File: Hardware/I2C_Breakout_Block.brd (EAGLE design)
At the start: 30.5 x 44.5 mm, 23 parts, among them U2 PCA9306

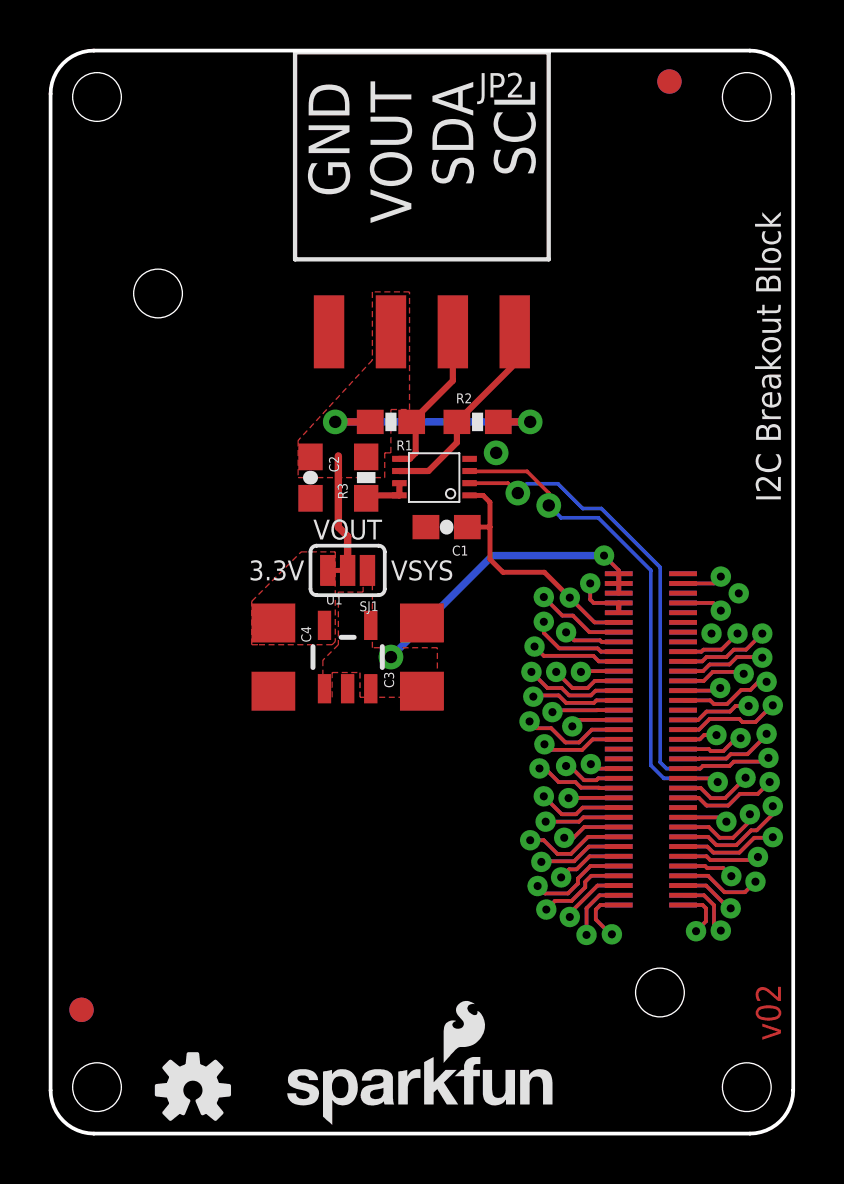
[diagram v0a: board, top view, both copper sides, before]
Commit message: repalced I2C resistors
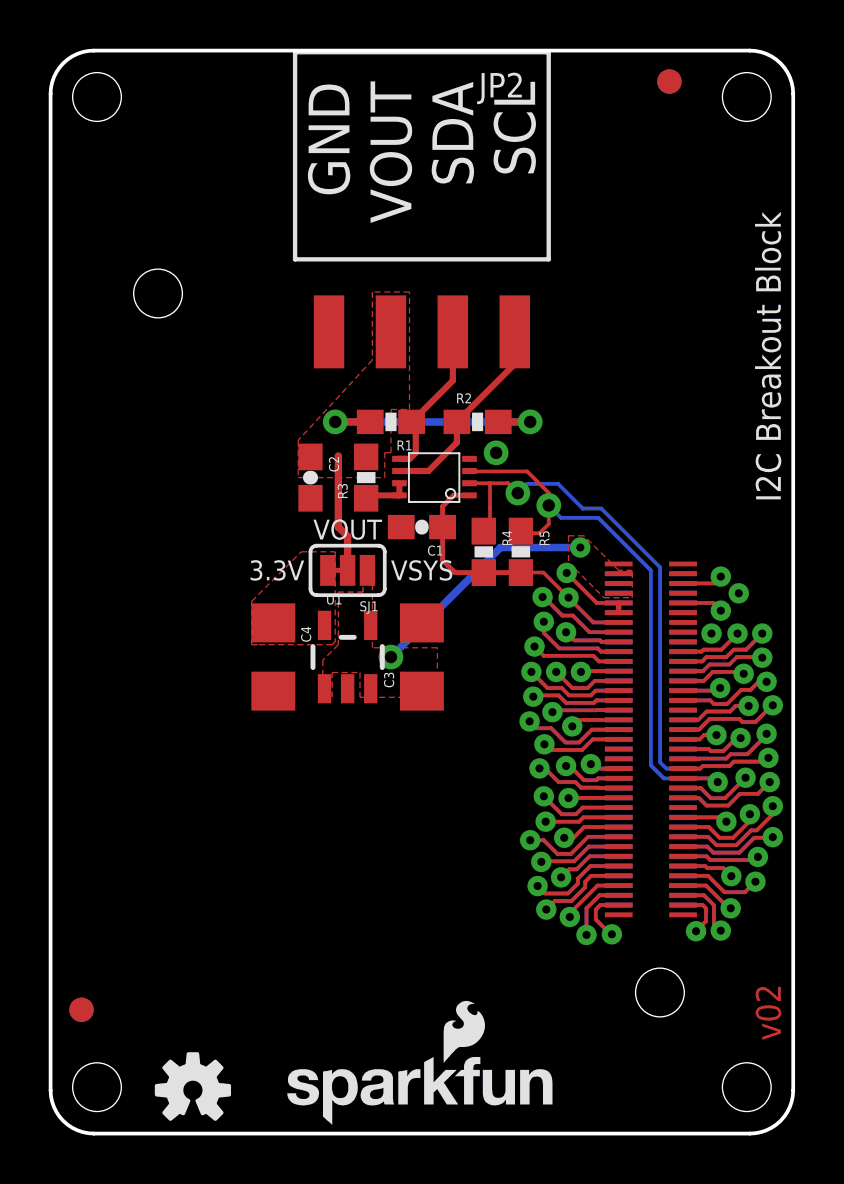
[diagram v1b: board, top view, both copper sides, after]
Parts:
- added R4, R5: DNP, SparkFun-Resistors:0603-RES
- moved C1 1.02 mm to (15.2, 24.9)
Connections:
- net 1.8V: now also R4.2, R5.2
- net GP19_I2C_1_SCL: now also R4.1
- net GP20_I2C_1_SDA: now also R5.1
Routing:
- net VSYS: track 14.2 -> 9.76 mm
- net GP20_I2C_1_SDA: track 21.9 -> 24.0 mm
- net GP19_I2C_1_SCL: track 26.0 -> 28.1 mm
- net 3.3V: track 4.98 -> 6.49 mm
- net 1.8V: track 13.0 -> 14.3 mm
